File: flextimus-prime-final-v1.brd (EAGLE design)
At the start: 78.7 x 65.7 mm, 40 parts, among them T1 2N2222, U1 STM32F042K6, U2 IP4220CZ6, U3 MCP1802T-3302I/OT

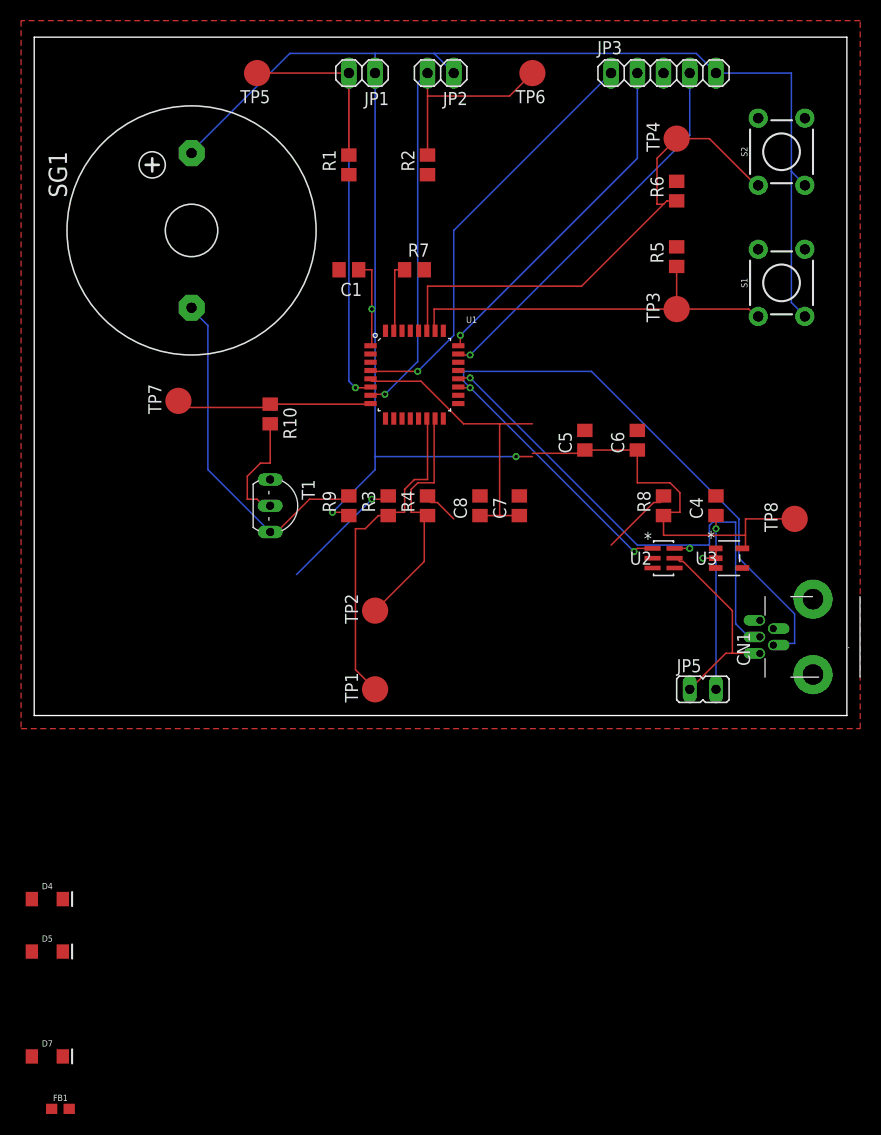
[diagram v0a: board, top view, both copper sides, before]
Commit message: Add new board layout and schematic
Also add new lcd driver to use later
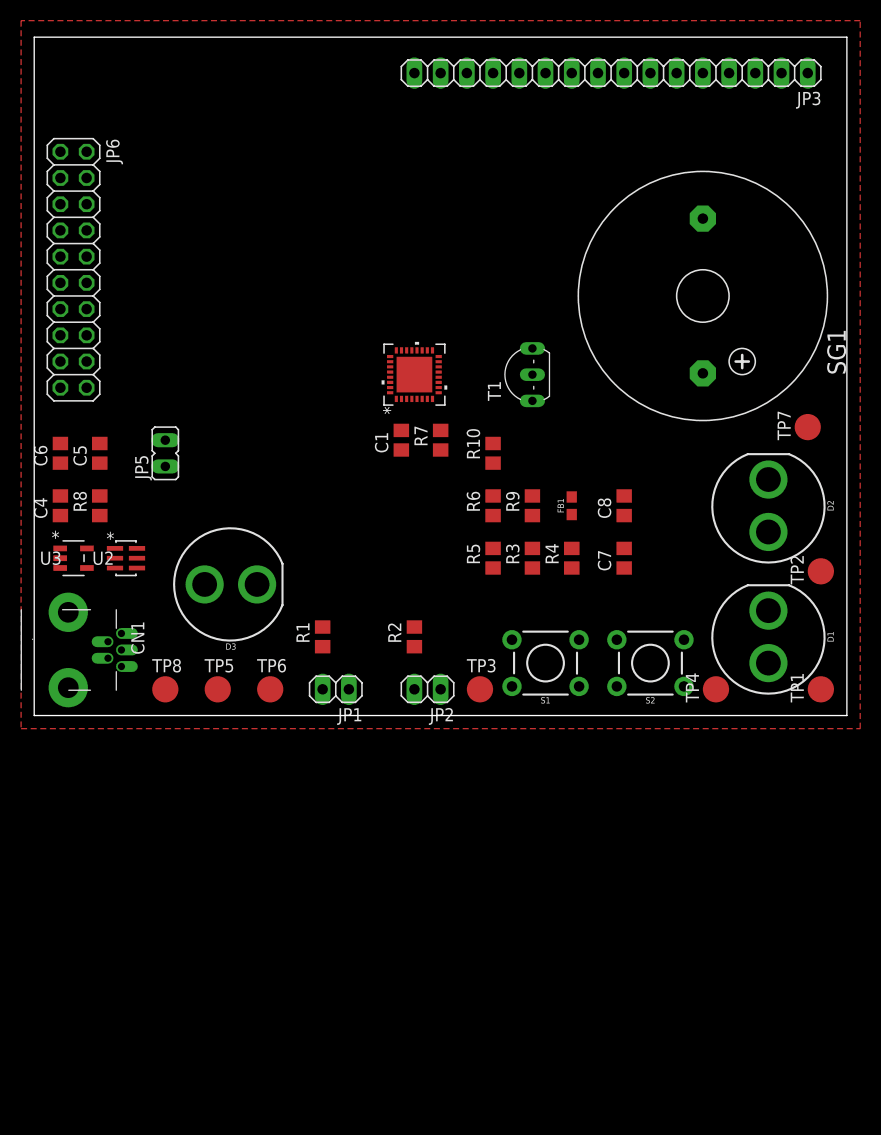
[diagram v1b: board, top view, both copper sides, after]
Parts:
- removed D4, D5, D7: BLUE, SparkFun-LED:LED-1206
- added D1, D2, D3: (no value), SparkFun-LED:LED_10MM
- added JP6: (no value), pinhead:2X10
- JP3: device pinhead:1X05 -> pinhead:1X16
- U1: value STM32F042K6 -> STM32F042KXU; device STM32F042K:QFP32-7X7 -> 411test:UFQFPN32-5X5MM
- moved CN1 81.3 mm to (-1.27, 6.35), turned to 270 degrees
- moved FB1 76.6 mm to (52.1, 20.3), turned to 90 degrees
- moved TP6 64.9 mm to (22.9, 2.54), turned to 0 degrees
- moved C4 63.5 mm to (2.54, 20.3)
- moved U3 63.5 mm to (3.81, 15.2)
- moved TP8 63.2 mm to (12.7, 2.54), turned to 0 degrees
- moved TP7 61.0 mm to (74.9, 27.9)
- moved TP5 59.8 mm to (17.8, 2.54), turned to 0 degrees
- moved JP1 59.7 mm to (29.2, 2.54)
- moved JP2 59.7 mm to (38.1, 2.54)
- moved JP5 56.9 mm to (12.7, 25.4), turned to 0 degrees
- moved C6 55.9 mm to (2.54, 25.4)
- moved R8 54.6 mm to (6.35, 20.3)
- moved TP4 53.5 mm to (66.0, 2.54)
- moved U2 52.1 mm to (8.89, 15.2)
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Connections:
- net BOOT0 renamed N$20
- removed net VDDIO2: U1.17
- new net N$10: JP3.4, U1.9
- new net N$11: JP3.5, U1.10
- new net N$12: JP3.6, U1.11
- new net N$13: JP3.7, U1.12
- new net N$14: JP3.8, U1.13
- new net N$15: JP3.9, U1.18
- new net N$16: JP3.10, U1.19
- new net N$17: JP3.11, U1.20
- new net N$18: JP3.12, U1.21
- new net N$19: JP3.13, U1.22
- new net N$4: JP3.14, U1.25
- net 3.3V: now also JP3.15, JP3.2, JP3.3, JP6.1, JP6.2, U1.17; no longer JP3.5
- net GND: now also D1.C, D2.C, D3.C, JP3.1, JP3.16, JP6.10, JP6.12, JP6.14, JP6.16, JP6.18, JP6.20, JP6.3, JP6.4, JP6.5, JP6.6, JP6.8, U1.33; no longer D4.C, D5.C, D7.C, JP3.3, U1.16, U1.32
- net N$5: now also D1.A; no longer D5.A
- net N$6: now also D2.A; no longer D4.A
- net N$9: now also D3.A; no longer D7.A
- net NRST: now also JP6.15; no longer JP3.1
- net SWCLK: now also JP6.9; no longer JP3.2
- net SWDIO: now also JP6.7; no longer JP3.4
- net USBM: no longer U1.20
- net USBP: no longer U1.19
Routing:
- net 3.3V: track 203.5 -> 0.00 mm, vias 3 -> 0
- net USBP: track 76.4 -> 0.00 mm, vias 2 -> 0
- net N$2: track 53.3 -> 0.00 mm, vias 1 -> 0
- net USBM: track 50.1 -> 0.00 mm, vias 2 -> 0
- net BUT2: track 49.4 -> 0.00 mm
- net N$1: track 49.1 -> 0.00 mm, vias 1 -> 0
- net NRST: track 41.2 -> 0.00 mm, vias 1 -> 0
- net BUT1: track 37.9 -> 0.00 mm
- net SWDIO: track 37.3 -> 0.00 mm, vias 1 -> 0
- net N$7: track 34.1 -> 0.00 mm
- net SWCLK: track 33.7 -> 0.00 mm, vias 1 -> 0
- net N$3: track 32.7 -> 0.00 mm
- net AVDD: track 30.2 -> 0.00 mm
- net N$21: track 24.8 -> 0.00 mm
- net +5V: track 20.3 -> 0.00 mm, vias 2 -> 0
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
